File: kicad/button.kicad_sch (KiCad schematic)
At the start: 4 parts

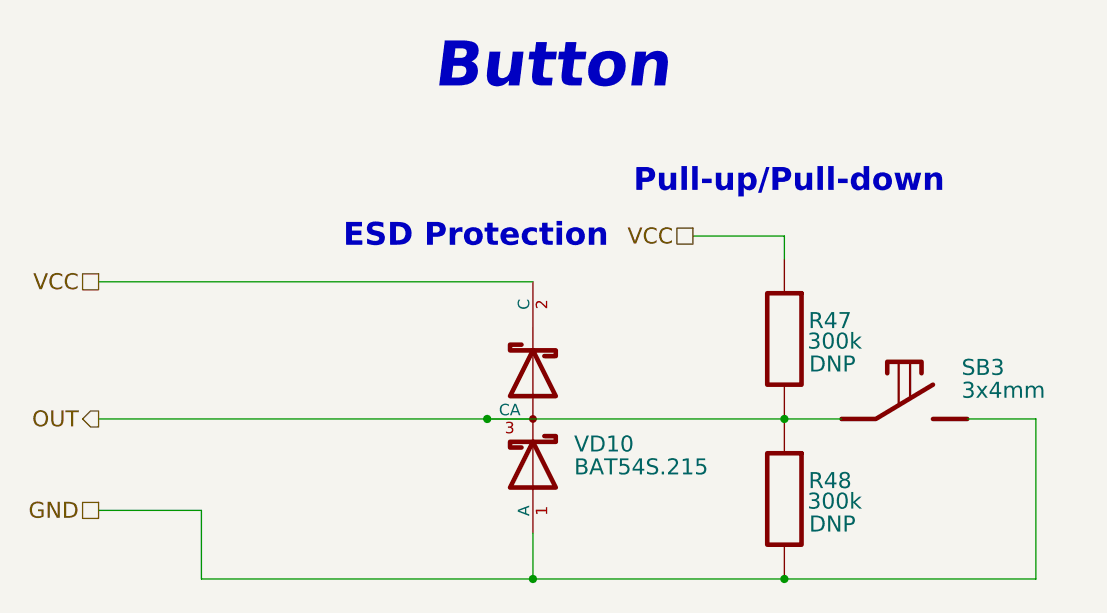
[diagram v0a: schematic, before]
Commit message: Reannotate schematic; Fix 5032 crystal footprint field; Update PCB with 5032 crystal
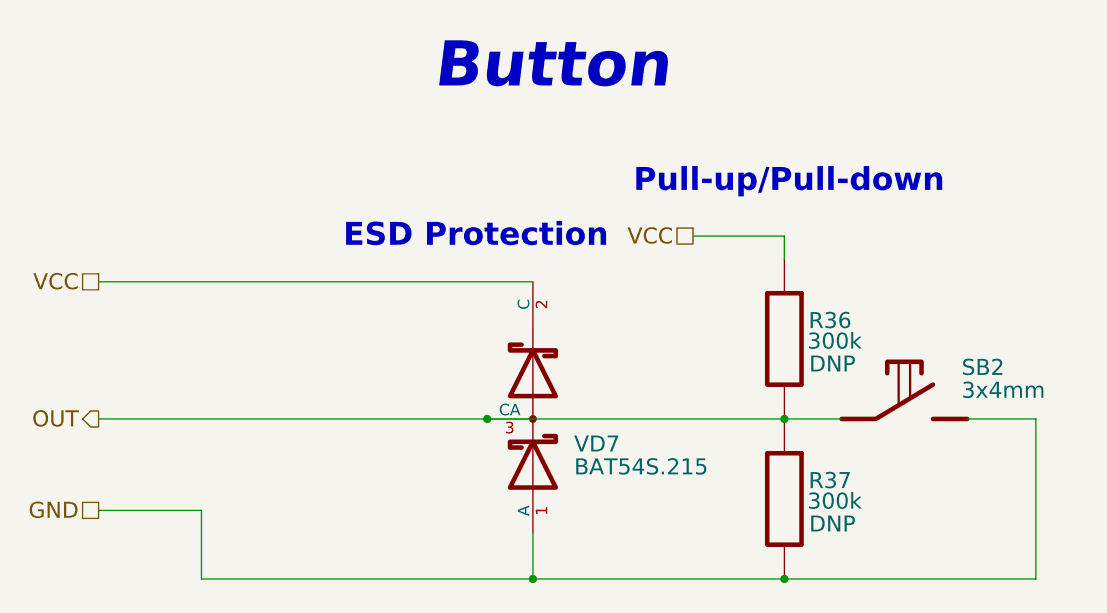
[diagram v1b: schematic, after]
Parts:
- renumbered R47 to R36, R48 to R37, SB3 to SB2, VD10 to VD7
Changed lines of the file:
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@@
   (symbol (lib_id "Resistors:R_RES") (at 179.578 109.22 270) (unit 1)
     (in_bom yes) (on_board yes)
-    (property "Reference" "R48" (id 0) (at 184.658 107.188 90)
+    (property "Reference" "R37" (id 0) (at 184.658 107.188 90)
       (effects (font (size 1.778 1.778)))
     )
@@
   (symbol (lib_id "Resistors:R_RES") (at 179.578 91.44 270) (unit 1)
     (in_bom yes) (on_board yes)
-    (property "Reference" "R47" (id 0) (at 184.658 89.408 90)
+    (property "Reference" "R36" (id 0) (at 184.658 89.408 90)
       (effects (font (size 1.778 1.778)))
     )
@@
   (symbol (lib_id "Diodes:VD_SCHOTTKY_PROTECT") (at 151.638 100.33 0) (unit 1)
     (in_bom yes) (on_board yes)
-    (property "Reference" "VD10" (id 0) (at 156.2101 103.124 0)
+    (property "Reference" "VD7" (id 0) (at 156.2101 103.124 0)
       (effects (font (size 1.778 1.778)) (justify left))
     )
@@
   (symbol (lib_id "Switches:SB_ON") (at 193.548 100.33 0) (unit 1)
     (in_bom yes) (on_board yes)
-    (property "Reference" "SB3" (id 0) (at 199.263 94.615 0)
+    (property "Reference" "SB2" (id 0) (at 199.263 94.615 0)
       (effects (font (size 1.778 1.778)) (justify left))
     )

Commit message: Add voltage value to caps, update BOM, SCH, ASM
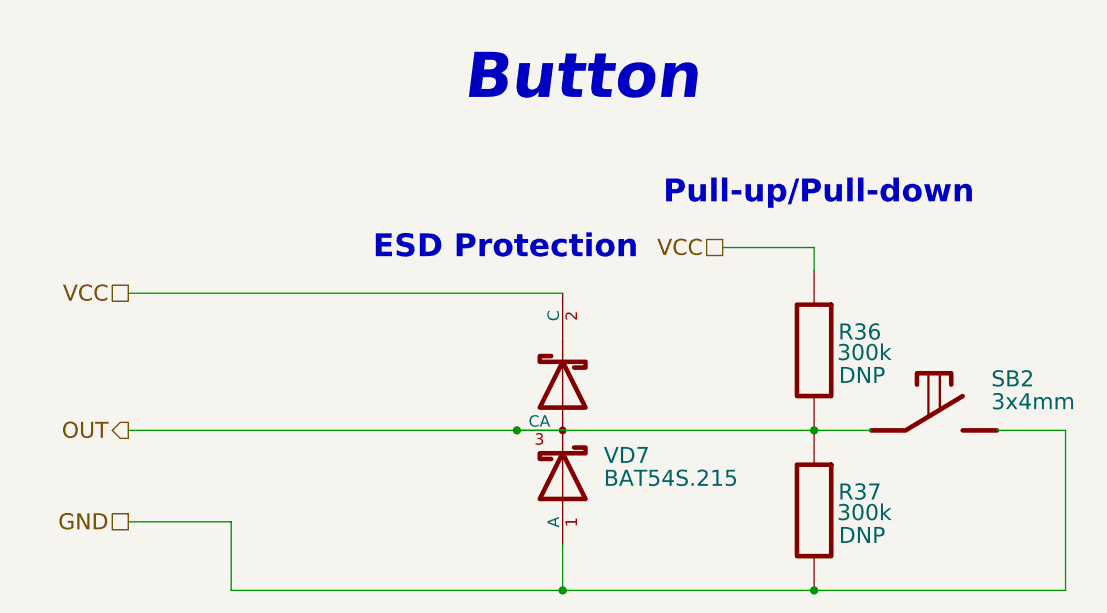
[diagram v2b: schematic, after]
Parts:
- R36, R37: Case/Package 0000 -> 0603; Tolerance ±% -> ±5%
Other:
- moved on the sheet: R36, R37, SB2, VD7
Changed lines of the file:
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@@
 (kicad_sch (version 20211123) (generator eeschema)
   (paper "A4")
-  (junction (at 179.578 118.11) (diameter 0) (color 0 0 0 0)
+  (junction (at 182.88 119.38) (diameter 0) (color 0 0 0 0)
   )
-  (junction (at 151.638 118.11) (diameter 0) (color 0 0 0 0)
+  (junction (at 154.94 119.38) (diameter 0) (color 0 0 0 0)
   )
-  (junction (at 146.558 100.33) (diameter 0) (color 0 0 0 0)
+  (junction (at 149.86 101.6) (diameter 0) (color 0 0 0 0)
   )
-  (junction (at 179.578 100.33) (diameter 0) (color 0 0 0 0)
+  (junction (at 182.88 101.6) (diameter 0) (color 0 0 0 0)
   )
-  (wire (pts (xy 179.578 80.01) (xy 179.578 82.55))
+  (wire (pts (xy 182.88 81.28) (xy 182.88 83.82))
     (stroke (width 0) (type default) (color 0 0 0 0))
   )
-  (wire (pts (xy 103.378 110.49) (xy 114.808 110.49))
+  (wire (pts (xy 106.68 111.76) (xy 118.11 111.76))
     (stroke (width 0) (type default) (color 0 0 0 0))
   )
-  (wire (pts (xy 169.418 80.01) (xy 179.578 80.01))
+  (wire (pts (xy 172.72 81.28) (xy 182.88 81.28))
     (stroke (width 0) (type default) (color 0 0 0 0))
   )
-  (wire (pts (xy 114.808 118.11) (xy 114.808 110.49))
+  (wire (pts (xy 118.11 119.38) (xy 118.11 111.76))
     (stroke (width 0) (type default) (color 0 0 0 0))
   )
-  (wire (pts (xy 207.518 100.33) (xy 199.898 100.33))
+  (wire (pts (xy 210.82 101.6) (xy 203.2 101.6))
     (stroke (width 0) (type default) (color 0 0 0 0))
   )
-  (wire (pts (xy 179.578 118.11) (xy 151.638 118.11))
+  (wire (pts (xy 182.88 119.38) (xy 154.94 119.38))
     (stroke (width 0) (type default) (color 0 0 0 0))
   )
-  (wire (pts (xy 151.638 118.11) (xy 114.808 118.11))
+  (wire (pts (xy 154.94 119.38) (xy 118.11 119.38))
     (stroke (width 0) (type default) (color 0 0 0 0))
   )
-  (wire (pts (xy 151.638 113.03) (xy 151.638 118.11))
+  (wire (pts (xy 154.94 114.3) (xy 154.94 119.38))
     (stroke (width 0) (type default) (color 0 0 0 0))
   )
-  (wire (pts (xy 179.578 100.33) (xy 185.928 100.33))
+  (wire (pts (xy 182.88 101.6) (xy 189.23 101.6))
     (stroke (width 0) (type default) (color 0 0 0 0))
   )
-  (wire (pts (xy 103.378 85.09) (xy 151.638 85.09))
+  (wire (pts (xy 106.68 86.36) (xy 154.94 86.36))
     (stroke (width 0) (type default) (color 0 0 0 0))
   )
-  (wire (pts (xy 207.518 100.33) (xy 207.518 118.11))
+  (wire (pts (xy 210.82 101.6) (xy 210.82 119.38))
     (stroke (width 0) (type default) (color 0 0 0 0))
   )
-  (wire (pts (xy 207.518 118.11) (xy 179.578 118.11))
+  (wire (pts (xy 210.82 119.38) (xy 182.88 119.38))
     (stroke (width 0) (type default) (color 0 0 0 0))
   )
-  (wire (pts (xy 146.558 100.33) (xy 179.578 100.33))
+  (wire (pts (xy 149.86 101.6) (xy 182.88 101.6))
     (stroke (width 0) (type default) (color 0 0 0 0))
   )
-  (wire (pts (xy 103.378 100.33) (xy 146.558 100.33))
+  (wire (pts (xy 106.68 101.6) (xy 149.86 101.6))
     (stroke (width 0) (type default) (color 0 0 0 0))
   )
-  (text "Pull-up/Pull-down" (at 162.814 75.438 0)
+  (text "Pull-up/Pull-down" (at 166.116 76.708 0)
     (effects (font (size 2.54 2.54) (thickness 0.508) bold) (justify left bottom))
   )
-  (text "ESD Protection" (at 130.556 81.534 0)
+  (text "ESD Protection" (at 133.858 82.804 0)
     (effects (font (size 2.54 2.54) (thickness 0.508) bold) (justify left bottom))
   )
-  (text "Button" (at 140.589 64.135 0)
+  (text "Button" (at 143.891 65.405 0)
     (effects (font (size 5.0038 5.0038) (thickness 1.0008) bold italic) (justify left bottom))
   )
-  (hierarchical_label "OUT" (shape output) (at 103.378 100.33 180)
+  (hierarchical_label "OUT" (shape output) (at 106.68 101.6 180)
     (effects (font (size 1.778 1.778)) (justify right))
   )
-  (hierarchical_label "VCC" (shape passive) (at 169.418 80.01 180)
+  (hierarchical_label "VCC" (shape passive) (at 172.72 81.28 180)
     (effects (font (size 1.778 1.778)) (justify right))
   )
-  (hierarchical_label "GND" (shape passive) (at 103.378 110.49 180)
+  (hierarchical_label "GND" (shape passive) (at 106.68 111.76 180)
     (effects (font (size 1.778 1.778)) (justify right))
   )
-  (hierarchical_label "VCC" (shape passive) (at 103.378 85.09 180)
+  (hierarchical_label "VCC" (shape passive) (at 106.68 86.36 180)
     (effects (font (size 1.778 1.778)) (justify right))
   )
-  (symbol (lib_id "Resistors:R_RES") (at 179.578 109.22 270) (unit 1)
+  (symbol (lib_id "Resistors:R_RES") (at 182.88 110.49 270) (unit 1)
     (in_bom yes) (on_board yes)
-    (property "Reference" "R37" (id 0) (at 184.658 107.188 90)
+    (property "Reference" "R37" (id 0) (at 187.96 108.458 90)
       (effects (font (size 1.778 1.778)))
     )
-    (property "Value" "300k" (id 1) (at 185.166 109.474 90)
+    (property "Value" "300k" (id 1) (at 188.468 110.744 90)
       (effects (font (size 1.778 1.778)))
     )
-    (property "Footprint" "Resistor_SMD:R_0603_1608Metric" (id 2) (at 179.578 109.22 0)
+    (property "Footprint" "Resistor_SMD:R_0603_1608Metric" (id 2) (at 182.88 110.49 0)
       (effects (font (size 1.778 1.778)) hide)
     )
-    (property "Datasheet" "" (id 3) (at 179.578 109.22 0)
+    (property "Datasheet" "" (id 3) (at 182.88 110.49 0)
       (effects (font (size 1.778 1.778)) hide)
     )
-    (property "Assembly" "DNP" (id 4) (at 184.912 112.014 90)
+    (property "Assembly" "DNP" (id 4) (at 188.214 113.284 90)
       (effects (font (size 1.778 1.778)))
     )
-    (property "Case/Package" "0000" (id 5) (at 173.228 109.22 0)
+    (property "Case/Package" "0603" (id 5) (at 176.53 110.49 0)
       (effects (font (size 1.27 1.27)) hide)
     )
-    (property "Power" "mW" (id 6) (at 171.704 109.22 0)
+    (property "Power" "mW" (id 6) (at 175.006 110.49 0)
       (effects (font (size 1.27 1.27)) hide)
     )
-    (property "Tolerance" "±%" (id 7) (at 169.926 109.22 0)
+    (property "Tolerance" "±5%" (id 7) (at 173.228 110.49 0)
       (effects (font (size 1.27 1.27)) hide)
     )
+    (property "Part Number" "" (id 8) (at 182.88 110.49 0))
     (pin "1")
     (pin "2")
   )
-  (symbol (lib_id "Resistors:R_RES") (at 179.578 91.44 270) (unit 1)
+  (symbol (lib_id "Resistors:R_RES") (at 182.88 92.71 270) (unit 1)
     (in_bom yes) (on_board yes)
-    (property "Reference" "R36" (id 0) (at 184.658 89.408 90)
+    (property "Reference" "R36" (id 0) (at 187.96 90.678 90)
       (effects (font (size 1.778 1.778)))
     )
-    (property "Value" "300k" (id 1) (at 185.166 91.694 90)
+    (property "Value" "300k" (id 1) (at 188.468 92.964 90)
       (effects (font (size 1.778 1.778)))
     )
-    (property "Footprint" "Resistor_SMD:R_0603_1608Metric" (id 2) (at 179.578 91.44 0)
+    (property "Footprint" "Resistor_SMD:R_0603_1608Metric" (id 2) (at 182.88 92.71 0)
       (effects (font (size 1.778 1.778)) hide)
     )
-    (property "Datasheet" "" (id 3) (at 179.578 91.44 0)
+    (property "Datasheet" "" (id 3) (at 182.88 92.71 0)
       (effects (font (size 1.778 1.778)) hide)
     )
-    (property "Assembly" "DNP" (id 4) (at 184.912 94.234 90)
+    (property "Assembly" "DNP" (id 4) (at 188.214 95.504 90)
       (effects (font (size 1.778 1.778)))
     )
-    (property "Case/Package" "0000" (id 5) (at 173.228 91.44 0)
+    (property "Case/Package" "0603" (id 5) (at 176.53 92.71 0)
       (effects (font (size 1.27 1.27)) hide)
     )
-    (property "Power" "mW" (id 6) (at 171.704 91.44 0)
+    (property "Power" "mW" (id 6) (at 175.006 92.71 0)
       (effects (font (size 1.27 1.27)) hide)
     )
-    (property "Tolerance" "±%" (id 7) (at 169.926 91.44 0)
+    (property "Tolerance" "±5%" (id 7) (at 173.228 92.71 0)
       (effects (font (size 1.27 1.27)) hide)
     )
+    (property "Part Number" "" (id 8) (at 182.88 92.71 0))
     (pin "1")
     (pin "2")
   )
-  (symbol (lib_id "Diodes:VD_SCHOTTKY_PROTECT") (at 151.638 100.33 0) (unit 1)
+  (symbol (lib_id "Diodes:VD_SCHOTTKY_PROTECT") (at 154.94 101.6 0) (unit 1)
     (in_bom yes) (on_board yes)
-    (property "Reference" "VD7" (id 0) (at 156.2101 103.124 0)
+    (property "Reference" "VD7" (id 0) (at 159.5121 104.394 0)
       (effects (font (size 1.778 1.778)) (justify left))
     )
-    (property "Value" "BAT54S.215" (id 1) (at 156.2101 105.664 0)
+    (property "Value" "BAT54S.215" (id 1) (at 159.5121 106.934 0)
       (effects (font (size 1.778 1.778)) (justify left))
     )
-    (property "Footprint" "Package_TO_SOT_SMD:SOT-23" (id 2) (at 149.098 105.41 90)
+    (property "Footprint" "Package_TO_SOT_SMD:SOT-23" (id 2) (at 152.4 106.68 90)
       (effects (font (size 1.778 1.778)) hide)
     )
-    (property "Datasheet" "" (id 3) (at 149.098 105.41 90)
+    (property "Datasheet" "" (id 3) (at 152.4 106.68 90)
       (effects (font (size 1.778 1.778)) hide)
     )
@@
     (pin "3")
   )
-  (symbol (lib_id "Switches:SB_ON") (at 193.548 100.33 0) (unit 1)
+  (symbol (lib_id "Switches:SB_ON") (at 196.85 101.6 0) (unit 1)
     (in_bom yes) (on_board yes)
-    (property "Reference" "SB2" (id 0) (at 199.263 94.615 0)
+    (property "Reference" "SB2" (id 0) (at 202.565 95.885 0)
       (effects (font (size 1.778 1.778)) (justify left))
     )
-    (property "Value" "3x4mm" (id 1) (at 199.263 97.155 0)
+    (property "Value" "3x4mm" (id 1) (at 202.565 98.425 0)
       (effects (font (size 1.778 1.778)) (justify left))
     )
-    (property "Footprint" "Button_Switch_SMD:SW_SPST_B3U-1000P" (id 2) (at 193.548 100.33 0)
+    (property "Footprint" "Button_Switch_SMD:SW_SPST_B3U-1000P" (id 2) (at 196.85 101.6 0)
       (effects (font (size 1.778 1.778)) hide)
     )
-    (property "Datasheet" "" (id 3) (at 193.548 100.33 0)
+    (property "Datasheet" "" (id 3) (at 196.85 101.6 0)
       (effects (font (size 1.778 1.778)) hide)
     )

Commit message: Add wiring diagram; Add work ours (stage 2); refactor folders
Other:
- title: (none) -> RadioSens v1
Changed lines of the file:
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@@
 (kicad_sch (version 20211123) (generator eeschema)
   (paper "A4")
+  (title_block
+    (title "RadioSens v1")
+    (comment 2 "Electrical Circuit")
+  )
   (junction (at 182.88 119.38) (diameter 0) (color 0 0 0 0)
   )
